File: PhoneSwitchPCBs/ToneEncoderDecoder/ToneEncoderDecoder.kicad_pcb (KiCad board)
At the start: 2 copper layers, 100 x 100 mm, 124 parts, among them IC1 XRA1203IG24TR-F, IC2 NXB0108PWJ, IC3 74HC4316, IC4 74HC4316, IC5 TL074*DT, IC6 TL074*DT, IC7 TL072, IC8 MT8870DN1, IC9 MT8870DN1, J1 Tone Bus, J2 Power + Control, Q1 XP231N02013R-G, Q2 XP231N02013R-G, Y1 3.579545 MHz

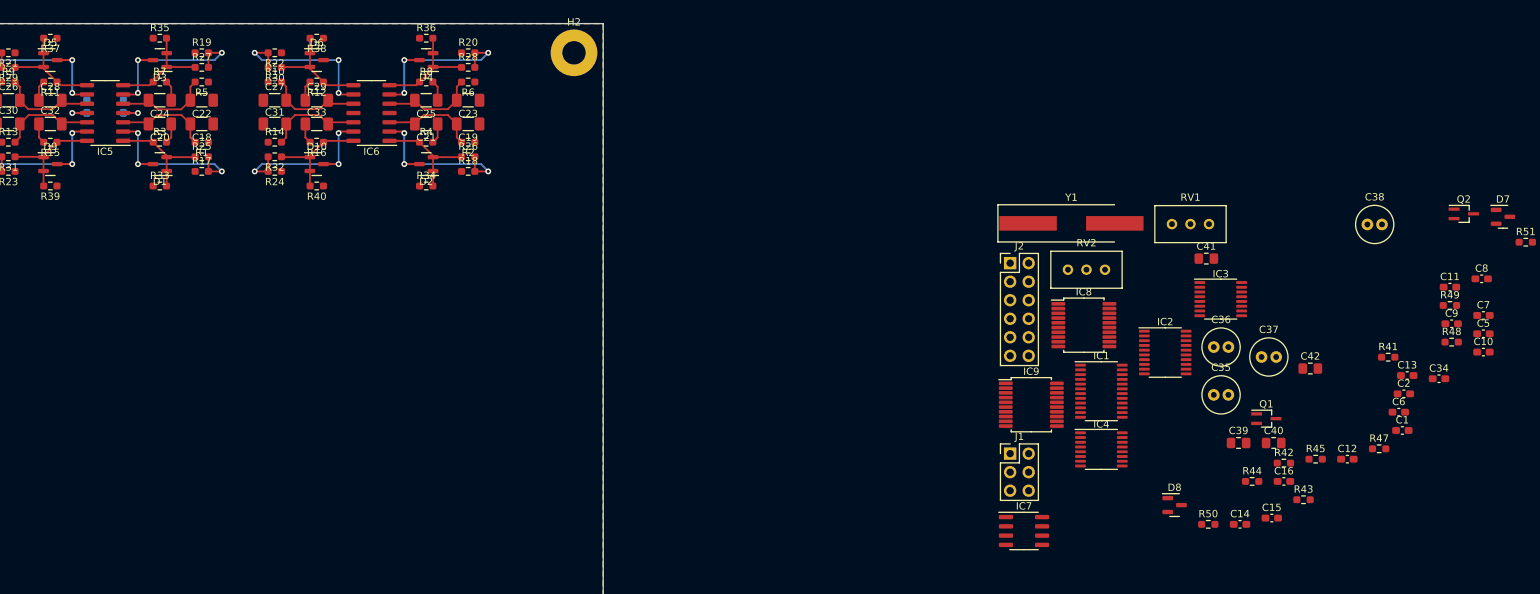
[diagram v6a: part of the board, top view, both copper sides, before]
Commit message: Power traces, among other things
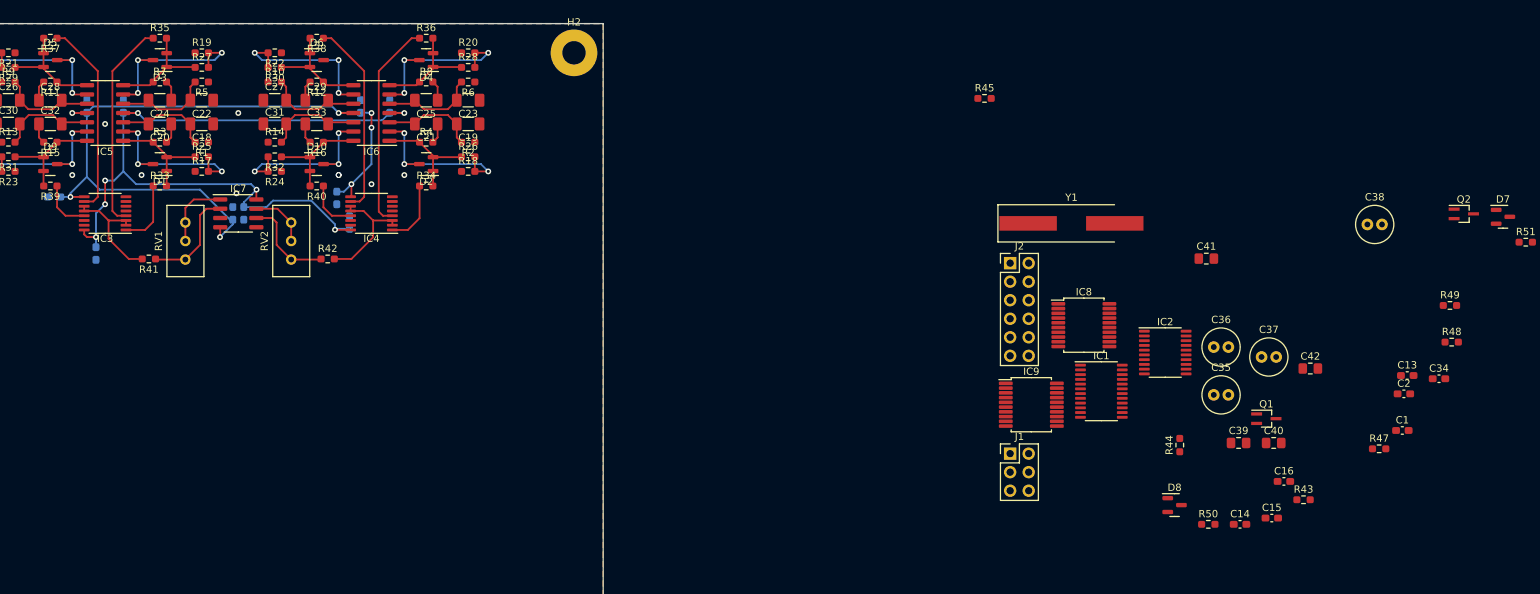
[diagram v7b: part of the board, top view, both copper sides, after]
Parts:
- C10, C11, C12, C5, C6, C7, C8, C9: moved to B.Cu
- moved C11 185.6 mm to (48.0, 49.0), turned to -90 degrees
- moved C12 180.8 mm to (42.2, 41.2)
- moved C5 170.7 mm to (68.2, 43.5), turned to -90 degrees
- moved R41 170.3 mm to (55.2, 49.8), turned to 180 degrees
- moved C6 162.1 mm to (66.8, 43.5), turned to -90 degrees
- moved C10 158.5 mm to (81.0, 41.4), turned to 90 degrees
- moved C8 155.4 mm to (84.2, 28.9), turned to -90 degrees
- moved IC3 153.3 mm to (49.2, 43.5), turned to 180 degrees
- moved C7 152.6 mm to (88.2, 28.9), turned to 90 degrees
- moved C9 151.6 mm to (82.8, 44.8), turned to 90 degrees
- moved RV1 140.3 mm to (60.2, 44.8), turned to 90 degrees
- moved R42 134.0 mm to (79.8, 49.8)
- moved IC7 116.1 mm to (67.5, 43.5)
- moved RV2 111.7 mm to (74.8, 44.8), turned to 90 degrees
- moved IC4 105.1 mm to (85.8, 43.5), turned to 180 degrees
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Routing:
- net +5VA: track 4.04 -> 109.4 mm, vias 1 -> 7
- net -5VA: track 4.04 -> 103.6 mm, vias 1 -> 7
- net Net-(IC4-Pad4): track 0.00 -> 28.8 mm
- net Net-(IC3-Pad4): track 0.00 -> 28.8 mm
- net Net-(IC4-Pad10): track 0.00 -> 26.8 mm
- net Net-(IC3-Pad10): track 0.00 -> 26.8 mm
- net Net-(IC4-Pad11): track 0.00 -> 16.4 mm
- net Net-(IC3-Pad11): track 0.00 -> 15.8 mm
- net Net-(IC7-Pad2): track 0.00 -> 14.2 mm
- net Net-(IC7-Pad6): track 0.00 -> 13.1 mm
- net /T1: track 0.00 -> 9.79 mm
- net Net-(IC3-Pad1): track 0.00 -> 9.10 mm
- net Net-(IC4-Pad1): track 0.00 -> 8.81 mm
- net /T2: track 0.00 -> 8.10 mm
- net Net-(IC4-Pad13): track 0.00 -> 7.12 mm
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
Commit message: More layout
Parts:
- C15, C16, D7, D8: moved to B.Cu
- moved D7 187.7 mm to (60.0, 94.4), turned to -90 degrees
- moved C13 175.7 mm to (52.0, 63.5)
- moved R47 172.4 mm to (52.0, 61.5), turned to 180 degrees
- moved C34 171.7 mm to (60.8, 78.5), turned to 180 degrees
- moved R43 168.3 mm to (46.5, 61.5), turned to 180 degrees
- moved R46 168.0 mm to (83.0, 63.5)
- moved R44 150.5 mm to (46.5, 63.5), turned to 0 degrees
- moved D8 150.1 mm to (46.0, 93.0), turned to 180 degrees
- moved C16 150.0 mm to (62.2, 59.6), turned to 180 degrees
- moved C15 149.7 mm to (62.2, 56.4), turned to 180 degrees
- moved R48 145.0 mm to (88.8, 61.5), turned to 180 degrees
- moved Y1 144.9 mm to (38.8, 68.8), turned to -90 degrees
- moved IC8 134.4 mm to (49.2, 68.2)
- moved Q2 128.2 mm to (108.0, 29.8), turned to 180 degrees
- moved IC2 127.1 mm to (67.5, 58.0), turned to 90 degrees
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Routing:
- net /T1: track 9.79 -> 86.5 mm, vias 0 -> 1
- net /620A: track 0.00 -> 41.0 mm
- net +5VD: track 0.00 -> 37.2 mm, vias 0 -> 2
- net /480B: track 0.00 -> 36.1 mm, vias 0 -> 2
- net /440B: track 0.00 -> 34.2 mm, vias 0 -> 2
- net /350A: track 0.00 -> 32.7 mm
- net /480A: track 0.00 -> 30.0 mm, vias 0 -> 2
- net /440A: track 0.00 -> 28.3 mm, vias 0 -> 2
- net /620B: track 0.00 -> 27.2 mm, vias 0 -> 2
- net /350B: track 0.00 -> 26.4 mm, vias 0 -> 2
- net Net-(C34-Pad2): track 0.00 -> 26.2 mm
- net Net-(C34-Pad1): track 0.00 -> 24.2 mm, vias 0 -> 2
- net /DB4: track 0.00 -> 22.6 mm
- net /DA4: track 0.00 -> 22.4 mm
- net /DA3: track 0.00 -> 22.4 mm
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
